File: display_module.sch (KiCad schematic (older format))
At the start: 113 parts, among them J4 46756-1001

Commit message: Started placing main components on PCB. Change of RT battery model and USB flash connector
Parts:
- gave numbers to parts that had none: 112

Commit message: Main components placed on board
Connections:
- net labels added: SoMtoDisplay_DATA_0, SoMtoDisplay_DATA_1, SoMtoDisplay_DATA_2, SoMtoDisplay_DATA_3, SoMtoDisplay_DATA_4, SoMtoDisplay_DATA_5, SoMtoDisplay_DATA_6, SoMtoDisplay_DATA_7, SoMtoDisplay_DATA_8, SoMtoDisplay_DATA_9, SoMtoDisplay_DATA_[0...9], SoMtoHDMI_DATA_0, SoMtoHDMI_DATA_1, SoMtoHDMI_DATA_2, SoMtoHDMI_DATA_3, SoMtoHDMI_DATA_4, SoMtoHDMI_DATA_5, SoMtoHDMI_DATA_6, SoMtoHDMI_DATA_7, SoMtoHDMI_DATA_8, SoMtoHDMI_DATA_9, SoMtoHDMI_DATA_[0...9]
- net labels removed: DSI0_CLK_N, DSI0_CLK_P, DSI0_LN0_N, DSI0_LN0_P, DSI0_LN1_N, DSI0_LN1_P, DSI0_LN2_N, DSI0_LN2_P, DSI0_LN3_N, DSI0_LN3_P, DSI1_CLK_N, DSI1_CLK_P, DSI1_LN0_N, DSI1_LN0_P, DSI1_LN1_N, DSI1_LN1_P, DSI1_LN2_N, DSI1_LN2_P, DSI1_LN3_N, DSI1_LN3_P, LT9611toHDMI_DATA, SoMtoDisplay_DATA, SoMtoHDMI_DATA
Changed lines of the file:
@@
 Wire Wire Line
 	6000 3550 5900 3550
-Entry Wire Line
-	4850 2800 4950 2900
-Wire Wire Line
-	4450 2100 4850 2100
-Entry Wire Line
-	4850 2100 4950 2200
-Entry Wire Line
-	4850 2200 4950 2300
-Entry Wire Line
-	4850 2300 4950 2400
-Entry Wire Line
-	4850 2500 4950 2600
-Entry Wire Line
-	4850 2600 4950 2700
-Entry Wire Line
-	4850 2700 4950 2800
 Text Label 4850 2100 2    50   ~ 0
 TX_D2_P
@@
 Text Label 4850 2800 2    50   ~ 0
 TX_CLK_N
-Text Label 4950 2100 0    50   ~ 0
-LT9611toHDMI_DATA
 Connection ~ 1900 7200
 Wire Wire Line
@@
 Wire Wire Line
 	4550 4900 4450 4900
+Wire Wire Line
+	3150 1350 3150 1250
+Wire Wire Line
+	4550 1750 4450 1750
+Wire Wire Line
+	3000 1550 3150 1550
+Wire Wire Line
+	4700 850  4450 850
+Wire Wire Line
+	4550 1450 4450 1450
+Wire Wire Line
+	4450 1550 4450 1450
+Wire Wire Line
+	3150 4900 2900 4900
+Text Label 2250 2250 0    50   ~ 0
+SoMtoHDMI_DATA_7
+Text Label 2250 2350 0    50   ~ 0
+SoMtoHDMI_DATA_6
+Text Label 2250 2450 0    50   ~ 0
+SoMtoHDMI_DATA_5
+Text Label 2250 2550 0    50   ~ 0
+SoMtoHDMI_DATA_4
+Text Label 2250 2650 0    50   ~ 0
+SoMtoHDMI_DATA_9
+Text Label 2250 2850 0    50   ~ 0
+SoMtoHDMI_DATA_3
+Text Label 2250 2950 0    50   ~ 0
+SoMtoHDMI_DATA_2
+Text Label 2250 3050 0    50   ~ 0
+SoMtoHDMI_DATA_1
+Text Label 2250 3150 0    50   ~ 0
+SoMtoHDMI_DATA_0
+Wire Wire Line
+	3150 2250 2250 2250
+Wire Wire Line
+	2250 2350 3150 2350
+Wire Wire Line
+	3150 2450 2250 2450
+Wire Wire Line
+	2250 2550 3150 2550
+Wire Wire Line
+	3150 2650 2250 2650
+Wire Wire Line
+	2250 2750 3150 2750
+Wire Wire Line
+	3150 2850 2250 2850
+Wire Wire Line
+	2250 2950 3150 2950
+Wire Wire Line
+	3150 3050 2250 3050
+Wire Wire Line
+	2250 3150 3150 3150
 Entry Wire Line
-	4850 2400 4950 2500
-Wire Wire Line
-	3150 1350 3150 1250
-Wire Wire Line
-	4550 1750 4450 1750
-Wire Wire Line
-	3000 1550 3150 1550
-Wire Wire Line
-	4700 850  4450 850
-Wire Wire Line
-	4550 1450 4450 1450
-Wire Wire Line
-	4450 1550 4450 1450
-Wire Wire Line
-	3150 4900 2900 4900
-Text Label 2650 2250 0    50   ~ 0
-DSI1_LN3_N
-Text Label 2650 2350 0    50   ~ 0
-DSI1_LN3_P
-Text Label 2650 2450 0    50   ~ 0
-DSI1_LN2_N
-Text Label 2650 2550 0    50   ~ 0
-DSI1_LN2_P
-Text Label 2650 2650 0    50   ~ 0
-DSI1_CLK_N
-Text Label 2650 2850 0    50   ~ 0
-DSI1_LN1_N
-Text Label 2650 2950 0    50   ~ 0
-DSI1_LN1_P
-Text Label 2650 3050 0    50   ~ 0
-DSI1_LN0_N
-Text Label 2650 3150 0    50   ~ 0
-DSI1_LN0_P
-Wire Wire Line
-	3150 2250 2650 2250
-Wire Wire Line
-	2650 2350 3150 2350
-Wire Wire Line
-	3150 2450 2650 2450
-Wire Wire Line
-	2650 2550 3150 2550
-Wire Wire Line
-	3150 2650 2650 2650
-Wire Wire Line
-	2650 2750 3150 2750
-Wire Wire Line
-	3150 2850 2650 2850
-Wire Wire Line
-	2650 2950 3150 2950
-Wire Wire Line
-	3150 3050 2650 3050
-Wire Wire Line
-	2650 3150 3150 3150
+	2150 2150 2250 2250
 Entry Wire Line
-	2550 2150 2650 2250
+	2150 2250 2250 2350
 Entry Wire Line
-	2550 2250 2650 2350
+	2150 2350 2250 2450
 Entry Wire Line
-	2550 2350 2650 2450
+	2150 2450 2250 2550
 Entry Wire Line
-	2550 2450 2650 2550
+	2150 2550 2250 2650
 Entry Wire Line
-	2550 2550 2650 2650
+	2150 2650 2250 2750
 Entry Wire Line
-	2550 2650 2650 2750
+	2150 2750 2250 2850
 Entry Wire Line
-	2550 2750 2650 2850
+	2150 2850 2250 2950
 Entry Wire Line
-	2550 2850 2650 2950
+	2150 2850 2250 2950
 Entry Wire Line
-	2550 2850 2650 2950
+	2150 2950 2250 3050
 Entry Wire Line
-	2550 2950 2650 3050
-Entry Wire Line
-	2550 3050 2650 3150
-Wire Bus Line
-	2550 2150 2500 2150
-Text GLabel 2500 2150 0    50   Input ~ 0
-SoMtoHDMI_DATA
+	2150 3050 2250 3150
+Text GLabel 2150 3050 0    50   Input ~ 0
+SoMtoHDMI_DATA_[0...9]
 Wire Wire Line
 	2950 850  3150 850
@@
 	1    0    0    -1
 $EndComp
-Text Label 2650 2750 0    50   ~ 0
-DSI1_CLK_P
-Text Label 1600 8500 0    50   ~ 0
-DSI0_LN3_N
-Text Label 1600 8600 0    50   ~ 0
-DSI0_LN3_P
-Text Label 1600 8800 0    50   ~ 0
-DSI0_LN2_N
-Text Label 1600 8900 0    50   ~ 0
-DSI0_LN2_P
-Text Label 1600 9700 0    50   ~ 0
-DSI0_CLK_N
-Text Label 1600 9800 0    50   ~ 0
-DSI0_CLK_P
-Text Label 1600 9100 0    50   ~ 0
-DSI0_LN1_N
-Text Label 1600 9200 0    50   ~ 0
-DSI0_LN1_P
-Text Label 1600 9400 0    50   ~ 0
-DSI0_LN0_N
-Text Label 1600 9500 0    50   ~ 0
-DSI0_LN0_P
+Text Label 2250 2750 0    50   ~ 0
+SoMtoHDMI_DATA_8
+Text Label 1400 8500 0    50   ~ 0
+SoMtoDisplay_DATA_7
+Text Label 1400 8600 0    50   ~ 0
+SoMtoDisplay_DATA_6
+Text Label 1400 8800 0    50   ~ 0
+SoMtoDisplay_DATA_5
+Text Label 1400 8900 0    50   ~ 0
+SoMtoDisplay_DATA_4
+Text Label 1400 9700 0    50   ~ 0
+SoMtoDisplay_DATA_9
+Text Label 1400 9800 0    50   ~ 0
+SoMtoDisplay_DATA_8
+Text Label 1400 9100 0    50   ~ 0
+SoMtoDisplay_DATA_3
+Text Label 1400 9200 0    50   ~ 0
+SoMtoDisplay_DATA_2
+Text Label 1400 9400 0    50   ~ 0
+SoMtoDisplay_DATA_1
+Text Label 1400 9500 0    50   ~ 0
+SoMtoDisplay_DATA_0
 Entry Wire Line
-	1500 8400 1600 8500
+	1300 8400 1400 8500
 Entry Wire Line
-	1500 8500 1600 8600
+	1300 8500 1400 8600
 Entry Wire Line
-	1500 8700 1600 8800
+	1300 8700 1400 8800
 Entry Wire Line
-	1500 8800 1600 8900
+	1300 8800 1400 8900
 Entry Wire Line
-	1500 9000 1600 9100
+	1300 9000 1400 9100
 Entry Wire Line
-	1500 9100 1600 9200
+	1300 9100 1400 9200
 Entry Wire Line
-	1500 9300 1600 9400
+	1300 9300 1400 9400
 Entry Wire Line
-	1500 9400 1600 9500
+	1300 9400 1400 9500
 Entry Wire Line
-	1500 9400 1600 9500
+	1300 9400 1400 9500
 Entry Wire Line
-	1500 9600 1600 9700
+	1300 9600 1400 9700
 Entry Wire Line
-	1500 9700 1600 9800
-Wire Bus Line
-	1500 8400 1450 8400
-Text GLabel 1450 8400 0    50   Input ~ 0
-SoMtoDisplay_DATA
-Wire Wire Line
-	1600 8500 2250 8500
-Wire Wire Line
-	1600 8600 2250 8600
-Wire Wire Line
-	1600 8800 2250 8800
-Wire Wire Line
-	1600 9100 2250 9100
-Wire Wire Line
-	1600 9400 2250 9400
-Wire Wire Line
-	1600 9700 2250 9700
-Wire Wire Line
-	1600 9800 2250 9800
-Wire Wire Line
-	1600 9500 2250 9500
-Wire Wire Line
-	1600 9200 2250 9200
-Wire Wire Line
-	1600 8900 2250 8900
-Entry Wire Line
-	6500 2600 6400 2700
-Entry Wire Line
-	6500 1200 6400 1300
-Entry Wire Line
-	6500 1400 6400 1500
-Entry Wire Line
-	6500 1600 6400 1700
-Entry Wire Line
-	6500 2000 6400 2100
-Entry Wire Line
-	6500 2200 6400 2300
-Entry Wire Line
-	6500 2400 6400 2500
+	1300 9700 1400 9800
+Text GLabel 1300 8400 0    50   Input ~ 0
+SoMtoDisplay_DATA_[0...9]
+Wire Wire Line
+	1400 8500 2250 8500
+Wire Wire Line
+	1400 8600 2250 8600
+Wire Wire Line
+	1400 8800 2250 8800
+Wire Wire Line
+	1400 9100 2250 9100
+Wire Wire Line
+	1400 9400 2250 9400
+Wire Wire Line
+	1400 9700 2250 9700
+Wire Wire Line
+	1400 9800 2250 9800
+Wire Wire Line
+	1400 9500 2250 9500
+Wire Wire Line
+	1400 9200 2250 9200
+Wire Wire Line
+	1400 8900 2250 8900
 Text Label 6500 1200 0    50   ~ 0
 TX_D2_P
@@
 Text Label 6500 2600 0    50   ~ 0
 TX_CLK_N
-Text Label 6300 1300 2    50   ~ 0
-LT9611toHDMI_DATA
-Entry Wire Line
-	6500 1800 6400 1900
 $Comp
 L sc606-baseboard:R_50R_0402 R63
@@
 	0    1    1    0
 $EndComp
-Wire Bus Line
-	6300 1300 6400 1300
 $Comp
 L sc606-baseboard:C_100n_0402 C74
@@
 	6500 1400 7200 1400
 Wire Wire Line
-	6500 1200 6900 1200
-Wire Wire Line
 	6900 1100 6900 1200
-Connection ~ 6900 1200
 Wire Wire Line
 	6900 1200 9200 1200
@@
 Wire Wire Line
 	14050 2850 14550 2850
+Connection ~ 6900 1200
+Wire Wire Line
+	6500 1200 6900 1200
+Wire Wire Line
+	4450 2100 4850 2100
 Wire Bus Line
-	4950 2100 4950 2900
+	1300 8400 1300 9700
 Wire Bus Line
-	6400 1300 6400 2700
-Wire Bus Line
-	1500 8400 1500 9700
-Wire Bus Line
-	2550 2150 2550 3050
+	2150 2150 2150 3050
 $EndSCHEMATC

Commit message: FFC and general display camera connectors distributed on board
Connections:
- net labels added: SoMtoDisplay_CLK_N, SoMtoDisplay_CLK_P, SoMtoDisplay_D0_N, SoMtoDisplay_D0_P, SoMtoDisplay_D1_N, SoMtoDisplay_D1_P, SoMtoDisplay_D2_N, SoMtoDisplay_D2_P, SoMtoDisplay_D3_N, SoMtoDisplay_D3_P, SoMtoDisplay_Ferr_CLK_N, SoMtoDisplay_Ferr_CLK_P, SoMtoDisplay_Ferr_D0_N, SoMtoDisplay_Ferr_D0_P, SoMtoDisplay_Ferr_D1_N, SoMtoDisplay_Ferr_D1_P, SoMtoDisplay_Ferr_D2_N, SoMtoDisplay_Ferr_D2_P, SoMtoDisplay_Ferr_D3_N, SoMtoDisplay_Ferr_D3_P, SoMtoLT_CLK_N, SoMtoLT_CLK_P, SoMtoLT_D0_N, SoMtoLT_D0_P, SoMtoLT_D1_N, SoMtoLT_D1_P, SoMtoLT_D2_N, SoMtoLT_D2_P, SoMtoLT_D3_N, SoMtoLT_D3_P, TX_CLK_C_N, TX_CLK_C_P, TX_CLK_Ferr_N, TX_CLK_Ferr_P, TX_D0_C_N, TX_D0_C_P, TX_D0_Ferr_N, TX_D0_Ferr_P, TX_D1_C_N, TX_D1_C_P, TX_D1_Ferr_N, TX_D1_Ferr_P, TX_D2_C_N, TX_D2_C_P, TX_D2_Ferr_N, TX_D2_Ferr_P
- net labels removed: SoMtoDisplay_DATA_0, SoMtoDisplay_DATA_1, SoMtoDisplay_DATA_2, SoMtoDisplay_DATA_3, SoMtoDisplay_DATA_4, SoMtoDisplay_DATA_5, SoMtoDisplay_DATA_6, SoMtoDisplay_DATA_7, SoMtoDisplay_DATA_8, SoMtoDisplay_DATA_9, SoMtoDisplay_DATA_[0...9], SoMtoHDMI_DATA_0, SoMtoHDMI_DATA_1, SoMtoHDMI_DATA_2, SoMtoHDMI_DATA_3, SoMtoHDMI_DATA_4, SoMtoHDMI_DATA_5, SoMtoHDMI_DATA_6, SoMtoHDMI_DATA_7, SoMtoHDMI_DATA_8, SoMtoHDMI_DATA_9, SoMtoHDMI_DATA_[0...9]
- wire segments 428 -> 408
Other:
- moved on the sheet: J3, L10, L11, L12, L8, L9

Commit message: Started rearrangement of components. USB connectors changed to 2xUSB-C
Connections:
- net labels removed: SCL_HDMI, SDA_HDMI
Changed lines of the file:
@@
 Wire Wire Line
 	2000 10700 2200 10700
-$Comp
-L sc606-baseboard:NFP0QHB242HS2D L8
-U 1 1 620D3E98
-P 1700 8550
-F 0 "L8" H 2050 8650 50  0000 C CNN
-F 1 "NFP0QHB242HS2D" H 2300 8550 50  0000 C CNN
-F 2 "sc606-baseboard-footprints:FIL_NFP0QHB242HS2D" H 1455 8880 50  0001 C CNN
-F 3 "https://www.farnell.com/datasheets/2616945.pdf" H 1700 8550 50  0001 C CNN
-F 4 "NFP0QHB242HS2D" H 1700 8867 50  0001 C CNN "MPN"
-F 5 "MURATA" H 1700 8776 50  0001 C CNN "Manufacturer"
-	1    1700 8550
-	1    0    0    -1
-$EndComp
 Wire Wire Line
 	3800 8500 2000 8500
@@
 Wire Wire Line
 	2000 8600 2000 8650
-$Comp
-L sc606-baseboard:NFP0QHB242HS2D L9
-U 1 1 620DCF56
-P 1700 8850
-F 0 "L9" H 2050 8950 50  0000 C CNN
-F 1 "NFP0QHB242HS2D" H 2300 8850 50  0000 C CNN
-F 2 "sc606-baseboard-footprints:FIL_NFP0QHB242HS2D" H 1455 9180 50  0001 C CNN
-F 3 "https://www.farnell.com/datasheets/2616945.pdf" H 1700 8850 50  0001 C CNN
-F 4 "NFP0QHB242HS2D" H 1700 9167 50  0001 C CNN "MPN"
-F 5 "MURATA" H 1700 9076 50  0001 C CNN "Manufacturer"
-	1    1700 8850
-	1    0    0    -1
-$EndComp
 Wire Wire Line
 	3800 8800 2000 8800
@@
 Wire Wire Line
 	2000 8900 2000 8950
-$Comp
-L sc606-baseboard:NFP0QHB242HS2D L10
-U 1 1 620DE4CE
-P 1700 9150
-F 0 "L10" H 2050 9250 50  0000 C CNN
-F 1 "NFP0QHB242HS2D" H 2300 9150 50  0000 C CNN
-F 2 "sc606-baseboard-footprints:FIL_NFP0QHB242HS2D" H 1455 9480 50  0001 C CNN
-F 3 "https://www.farnell.com/datasheets/2616945.pdf" H 1700 9150 50  0001 C CNN
-F 4 "NFP0QHB242HS2D" H 1700 9467 50  0001 C CNN "MPN"
-F 5 "MURATA" H 1700 9376 50  0001 C CNN "Manufacturer"
-	1    1700 9150
-	1    0    0    -1
-$EndComp
 Wire Wire Line
 	3800 9100 2000 9100
@@
 Wire Wire Line
 	2000 9200 2000 9250
-$Comp
-L sc606-baseboard:NFP0QHB242HS2D L11
-U 1 1 620E0175
-P 1700 9450
-F 0 "L11" H 2050 9550 50  0000 C CNN
-F 1 "NFP0QHB242HS2D" H 2300 9450 50  0000 C CNN
-F 2 "sc606-baseboard-footprints:FIL_NFP0QHB242HS2D" H 1455 9780 50  0001 C CNN
-F 3 "https://www.farnell.com/datasheets/2616945.pdf" H 1700 9450 50  0001 C CNN
-F 4 "NFP0QHB242HS2D" H 1700 9767 50  0001 C CNN "MPN"
-F 5 "MURATA" H 1700 9676 50  0001 C CNN "Manufacturer"
-	1    1700 9450
-	1    0    0    -1
-$EndComp
 Wire Wire Line
 	3800 9400 2000 9400
@@
 F 5 "MURATA" H 1700 9976 50  0001 C CNN "Manufacturer"
 	1    1700 9750
-	1    0    0    -1
+	1    0    0    1
 $EndComp
 Wire Wire Line
@@
 CEC
 Text Label 5750 4150 2    50   ~ 0
-SCL_HDMI
+LTtoHDMI_SCL
 Text Label 5750 4250 2    50   ~ 0
-SDA_HDMI
+LTtoHDMI_SDA
 Wire Wire Line
 	5750 4150 5900 4150
@@
 Text Label 2750 9800 0    50   ~ 0
 SoMtoDisplay_Ferr_CLK_P
+$Comp
+L sc606-baseboard:NFP0QHB242HS2D L8
+U 1 1 620D3E98
+P 1700 8550
+F 0 "L8" H 2050 8650 50  0000 C CNN
+F 1 "NFP0QHB242HS2D" H 2300 8550 50  0000 C CNN
+F 2 "sc606-baseboard-footprints:FIL_NFP0QHB242HS2D" H 1455 8880 50  0001 C CNN
+F 3 "https://www.farnell.com/datasheets/2616945.pdf" H 1700 8550 50  0001 C CNN
+F 4 "NFP0QHB242HS2D" H 1700 8867 50  0001 C CNN "MPN"
+F 5 "MURATA" H 1700 8776 50  0001 C CNN "Manufacturer"
+	1    1700 8550
+	1    0    0    1
+$EndComp
+$Comp
+L sc606-baseboard:NFP0QHB242HS2D L11
+U 1 1 620E0175
+P 1700 9450
+F 0 "L11" H 2050 9550 50  0000 C CNN
+F 1 "NFP0QHB242HS2D" H 2300 9450 50  0000 C CNN
+F 2 "sc606-baseboard-footprints:FIL_NFP0QHB242HS2D" H 1455 9780 50  0001 C CNN
+F 3 "https://www.farnell.com/datasheets/2616945.pdf" H 1700 9450 50  0001 C CNN
+F 4 "NFP0QHB242HS2D" H 1700 9767 50  0001 C CNN "MPN"
+F 5 "MURATA" H 1700 9676 50  0001 C CNN "Manufacturer"
+	1    1700 9450
+	1    0    0    1
+$EndComp
+$Comp
+L sc606-baseboard:NFP0QHB242HS2D L10
+U 1 1 620DE4CE
+P 1700 9150
+F 0 "L10" H 2050 9250 50  0000 C CNN
+F 1 "NFP0QHB242HS2D" H 2300 9150 50  0000 C CNN
+F 2 "sc606-baseboard-footprints:FIL_NFP0QHB242HS2D" H 1455 9480 50  0001 C CNN
+F 3 "https://www.farnell.com/datasheets/2616945.pdf" H 1700 9150 50  0001 C CNN
+F 4 "NFP0QHB242HS2D" H 1700 9467 50  0001 C CNN "MPN"
+F 5 "MURATA" H 1700 9376 50  0001 C CNN "Manufacturer"
+	1    1700 9150
+	1    0    0    1
+$EndComp
+$Comp
+L sc606-baseboard:NFP0QHB242HS2D L9
+U 1 1 620DCF56
+P 1700 8850
+F 0 "L9" H 2050 8950 50  0000 C CNN
+F 1 "NFP0QHB242HS2D" H 2300 8850 50  0000 C CNN
+F 2 "sc606-baseboard-footprints:FIL_NFP0QHB242HS2D" H 1455 9180 50  0001 C CNN
+F 3 "https://www.farnell.com/datasheets/2616945.pdf" H 1700 8850 50  0001 C CNN
+F 4 "NFP0QHB242HS2D" H 1700 9167 50  0001 C CNN "MPN"
+F 5 "MURATA" H 1700 9076 50  0001 C CNN "Manufacturer"
+	1    1700 8850
+	1    0    0    1
+$EndComp
 $EndSCHEMATC

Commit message: All components placed on board
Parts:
- removed D9: S1G, sc606-baseboard-footprints:DO-214AC, symbol sc606-baseboard:S1G
- added D9: 1N4148W-7-F, antmicro-footprints:SOD-123, symbol antmicroDiodesRectifiersSingle:1N4148W-7-F
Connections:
- net labels added: SoMtoLT_SCL
- net labels removed: CEC, SoMtoLT__SCL, SoMtoLT__SDA
- wire segments 408 -> 413
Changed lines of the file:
@@
 $EndComp
 Text Label 1200 1950 2    50   ~ 0
-SoMtoLT__SDA
+SoMtoLT_SDA
 Text Label 1200 1850 2    50   ~ 0
-SoMtoLT__SCL
+SoMtoLT_SCL
 $Comp
 L sc606-baseboard:R_4k7_0402 R51
@@
 F 5 "MURATA" H 12700 1526 50  0001 C CNN "Manufacturer"
 	1    12700 1300
-	1    0    0    -1
-$EndComp
-Wire Wire Line
-	15150 1250 13300 1250
+	1    0    0    1
+$EndComp
 Wire Wire Line
 	13000 1250 13000 1200
-Wire Wire Line
-	15150 1350 13200 1350
 Wire Wire Line
 	13000 1350 13000 1400
@@
 F 5 "MURATA" H 12700 1826 50  0001 C CNN "Manufacturer"
 	1    12700 1600
-	1    0    0    -1
+	1    0    0    1
 $EndComp
 Wire Wire Line
@@
 F 5 "MURATA" H 12700 2126 50  0001 C CNN "Manufacturer"
 	1    12700 1900
-	1    0    0    -1
-$EndComp
-Wire Wire Line
-	15150 1850 13700 1850
+	1    0    0    1
+$EndComp
 Wire Wire Line
 	13000 1850 13000 1800
-Wire Wire Line
-	15150 1950 13600 1950
 Wire Wire Line
 	13000 1950 13000 2000
@@
 F 5 "MURATA" H 12700 2426 50  0001 C CNN "Manufacturer"
 	1    12700 2200
-	1    0    0    -1
+	1    0    0    1
 $EndComp
 Wire Wire Line
@@
 	4450 2000 4550 2000
 Text Label 5750 4350 2    50   ~ 0
-CEC
+CEC_HDMI
 Text Label 5750 4150 2    50   ~ 0
 LTtoHDMI_SCL
@@
 	9200 4550 9350 4550
 Text Label 10850 5150 0    50   ~ 0
-SoMtoLT__SCL
+SoMtoLT_SCL
 NoConn ~ 3150 3350
 NoConn ~ 3150 3450
@@
 F 6 "27k" V 10753 9570 50  0000 L CNN "Val"
 	1    10700 9500
-	0    1    1    0
-$EndComp
-$Comp
-L sc606-baseboard:S1G D9
-U 1 1 664DAA21
-P 10700 9150
-F 0 "D9" V 10647 9228 60  0000 L CNN
-F 1 "S1G" V 10753 9228 60  0000 L CNN
-F 2 "sc606-baseboard-footprints:DO-214AC" H 10900 9350 60  0001 L CNN
-F 3 "https://www.onsemi.com/pub/Collateral/S1M-D.pdf" H 10900 9450 60  0001 L CNN
-F 4 "S1G" H 10900 9650 60  0001 L CNN "MPN"
-F 5 "ON Semiconductor" H 10900 10250 60  0001 L CNN "Manufacturer"
-	1    10700 9150
 	0    1    1    0
 $EndComp
@@
 	13100 2150 13000 2150
 Wire Wire Line
-	13200 2500 13200 1350
-Connection ~ 13200 1350
-Wire Wire Line
-	13200 1350 13000 1350
-Wire Wire Line
-	13300 2500 13300 1250
-Connection ~ 13300 1250
-Wire Wire Line
-	13300 1250 13000 1250
-Wire Wire Line
 	13400 2500 13400 1650
 Connection ~ 13400 1650
@@
 Wire Wire Line
 	13500 1550 13000 1550
-Wire Wire Line
-	13600 2500 13600 1950
-Connection ~ 13600 1950
-Wire Wire Line
-	13600 1950 13000 1950
-Wire Wire Line
-	13700 2500 13700 1850
-Connection ~ 13700 1850
-Wire Wire Line
-	13700 1850 13000 1850
 $Comp
 L sc606-baseboard:GND #PWR078
@@
 	1    0    0    1
 $EndComp
+Wire Wire Line
+	13000 2500 13000 2300
+Connection ~ 13000 2300
+Wire Wire Line
+	13000 1950 13200 1950
+Wire Wire Line
+	13000 1850 13300 1850
+Wire Wire Line
+	13000 1350 13600 1350
+Wire Wire Line
+	13000 1250 13700 1250
+Wire Wire Line
+	13200 2500 13200 1950
+Connection ~ 13200 1950
+Wire Wire Line
+	13200 1950 15150 1950
+Wire Wire Line
+	13300 1850 13300 2500
+Connection ~ 13300 1850
+Wire Wire Line
+	13300 1850 15150 1850
+Wire Wire Line
+	13600 2500 13600 1350
+Connection ~ 13600 1350
+Wire Wire Line
+	13600 1350 15150 1350
+Wire Wire Line
+	13700 1250 13700 2500
+Connection ~ 13700 1250
+Wire Wire Line
+	13700 1250 15150 1250
+Wire Wire Line
+	3150 950  3150 850
+Connection ~ 3150 950
+Connection ~ 3150 850
+Wire Wire Line
+	4450 1050 4450 950
+Connection ~ 4450 850
+Connection ~ 4450 950
+Wire Wire Line
+	4450 950  4450 850
+Wire Wire Line
+	4450 1150 4450 1050
+Connection ~ 4450 1150
+Connection ~ 4450 1050
+$Comp
+L antmicroDiodesRectifiersSingle:1N4148W-7-F D9
+U 1 1 62B067B7
+P 10700 9150
+F 0 "D9" V 10647 9228 60  0000 L CNN
+F 1 "1N4148W-7-F" V 10753 9228 60  0000 L CNN
+F 2 "antmicro-footprints:SOD-123" H 10900 9350 60  0001 L CNN
+F 3 "https://www.diodes.com/assets/Datasheets/ds30086.pdf" H 10900 9450 60  0001 L CNN
+F 4 "1N4148W-7-F" H 10900 9650 60  0001 L CNN "MPN"
+F 5 "Diodes Incorporated" H 10900 10250 60  0001 L CNN "Manufacturer"
+	1    10700 9150
+	0    1    1    0
+$EndComp
 $EndSCHEMATC

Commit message: Finished placement after shortening board by 1cm
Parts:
- removed C83, C84: C_100n_0402, sc606-baseboard-footprints:0402-cap, symbol sc606-baseboard:C_100n_0402
- removed D6, D7, D8: TPD1E10B06DPYR, sc606-baseboard-footprints:XDFN-2_1x0.60mm, symbol sc606-baseboard:TPD1E10B06DPYR
- removed U9: TPD13S523PWR, sc606-baseboard-footprints:TSSOP-16, symbol sc606-baseboard:TPD13S523PWR
- added D29, D30, D6: PUSB3F96X_PASS, sc606-baseboard-footprints:PUSB3F96X, symbol sc606-baseboard:PUSB3F96X_PASS
- R90: DNP (none) -> DNP
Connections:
- wire segments 413 -> 375
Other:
- moved on the sheet: D10

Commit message: Changed USB flash and debug to USB-C. Prepared place for USB PD. Minor modifications of components position
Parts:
- D9: footprint antmicro-footprints:SOD-123 -> sc606-baseboard-footprints:SOD-123; symbol antmicroDiodesRectifiersSingle:1N4148W-7-F -> sc606-baseboard:1N4148W-7-F
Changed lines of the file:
@@
 $Descr A3 16535 11693
 encoding utf-8
-Sheet 5 8
+Sheet 5 9
 Title ""
 Date "2022-01-04"
@@
 Connection ~ 4450 1050
 $Comp
-L antmicroDiodesRectifiersSingle:1N4148W-7-F D9
+L sc606-baseboard:1N4148W-7-F D9
 U 1 1 62B067B7
 P 10700 9150
 F 0 "D9" V 10647 9228 60  0000 L CNN
 F 1 "1N4148W-7-F" V 10753 9228 60  0000 L CNN
-F 2 "antmicro-footprints:SOD-123" H 10900 9350 60  0001 L CNN
+F 2 "sc606-baseboard-footprints:SOD-123" H 10900 9350 60  0001 L CNN
 F 3 "https://www.diodes.com/assets/Datasheets/ds30086.pdf" H 10900 9450 60  0001 L CNN
 F 4 "1N4148W-7-F" H 10900 9650 60  0001 L CNN "MPN"

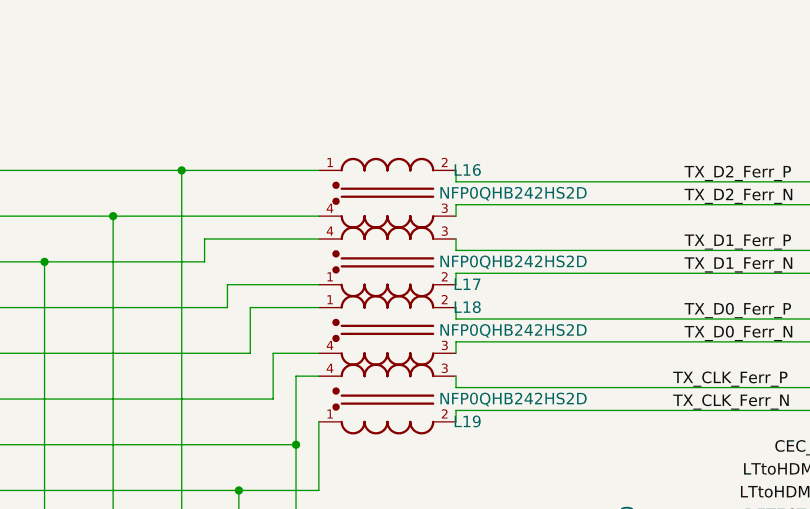
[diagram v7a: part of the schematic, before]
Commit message: Connecting LT9611
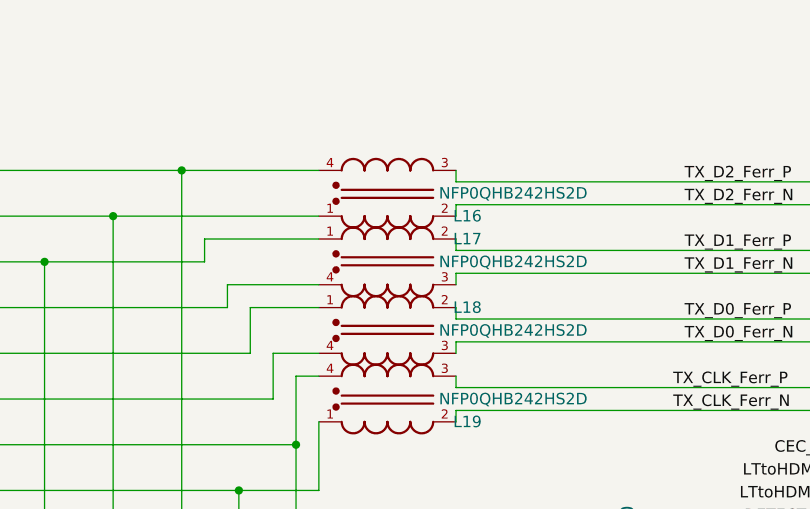
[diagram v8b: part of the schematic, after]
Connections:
- net TX_D1_C_N: now also L17.4; no longer L17.1
- net TX_D1_C_P: now also L17.1; no longer L17.4
- net TX_D1_Ferr_N: now also L17.3; no longer L17.2
- net TX_D1_Ferr_P: now also L17.2; no longer L17.3
- net TX_D2_C_N: now also L16.1; no longer L16.4
- net TX_D2_C_P: now also L16.4; no longer L16.1
- net TX_D2_Ferr_N: now also L16.2; no longer L16.3
- net TX_D2_Ferr_P: now also L16.3; no longer L16.2
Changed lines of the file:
@@
 F 5 "MURATA" H 12700 1526 50  0001 C CNN "Manufacturer"
 	1    12700 1300
-	1    0    0    -1
+	1    0    0    1
 $EndComp
 Wire Wire Line
@@
 F 5 "MURATA" H 12700 1826 50  0001 C CNN "Manufacturer"
 	1    12700 1600
-	1    0    0    1
+	1    0    0    -1
 $EndComp
 Wire Wire Line
